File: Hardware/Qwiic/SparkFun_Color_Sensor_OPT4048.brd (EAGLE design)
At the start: 25.4 x 25.4 mm, 40 parts, among them J1 QWIIC_RIGHT_ANGLE, J2 QWIIC_RIGHT_ANGLE

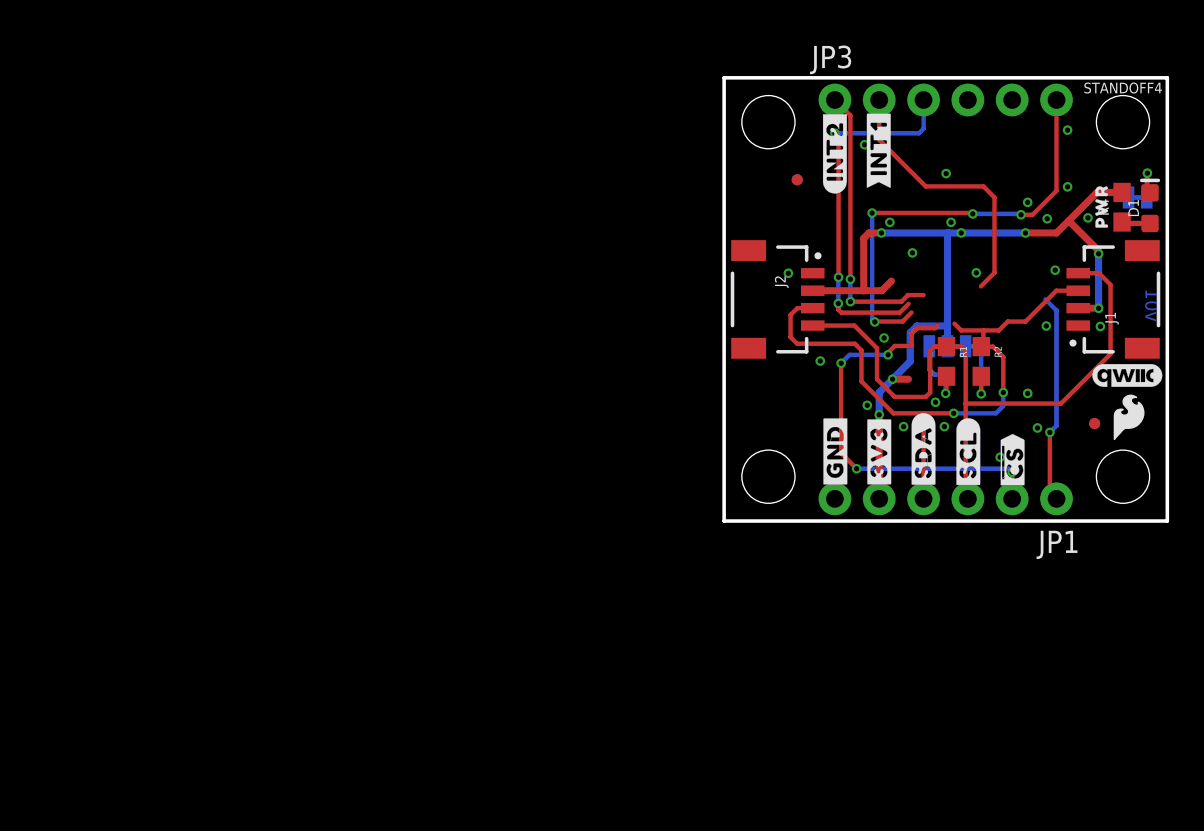
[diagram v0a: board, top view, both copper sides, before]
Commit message: Removes micro outline, adds mini outline
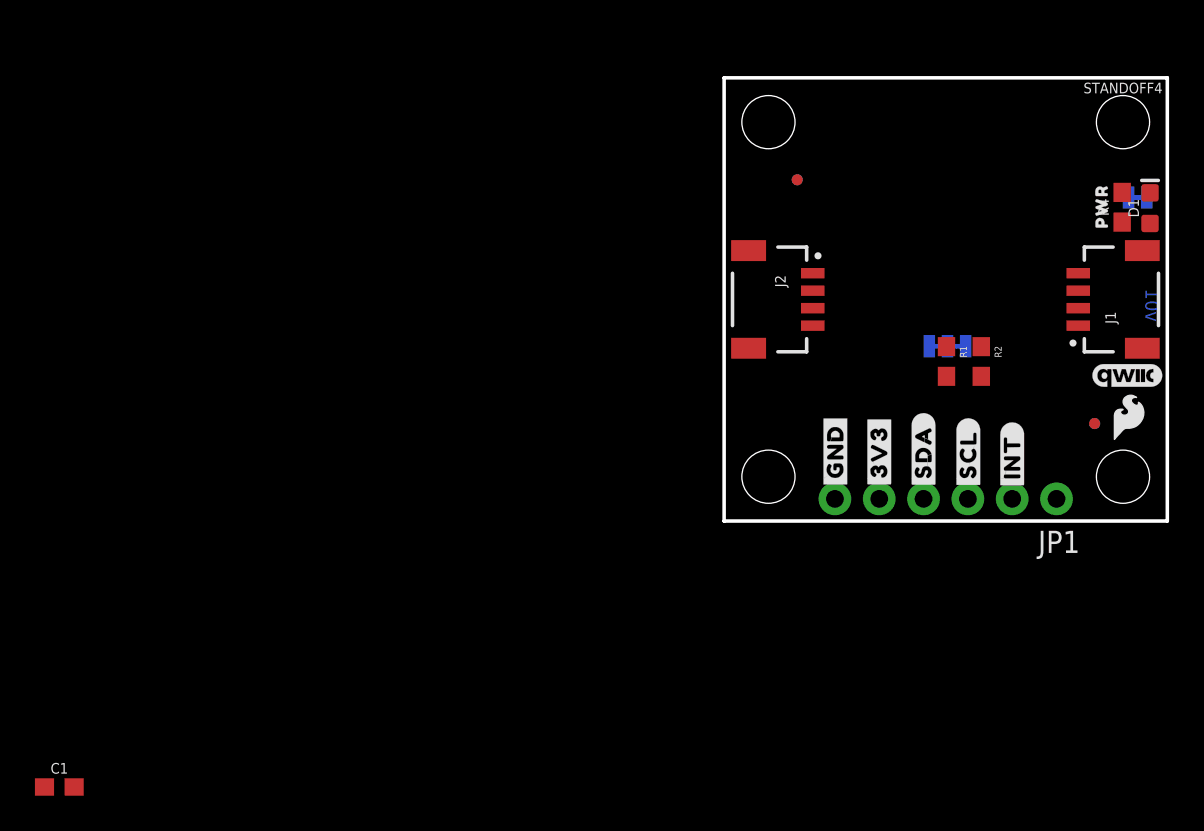
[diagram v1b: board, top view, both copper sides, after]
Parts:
- removed JP3: IO, SparkFun-Connectors:1X06_NO_SILK
- removed U$19: (no value), bot:#INT1#9
- removed U$26: (no value), ISMTop:#PICO#13
- removed U$27: (no value), bot:##CS##8
- removed U$40: (no value), top:#INT2#3
- removed U$8: (no value), top:#INT2#2
- added C1: 0.1uF, SparkFun-Capacitors:0603
- added U$6: (no value), bot:#INT#3
- U$3: device top:##CS##7 -> bot:#SDA#1
- U$7: device top:#INT1#9 -> top:#INT#9
- moved U$7 19.3 mm to (16.5, 3.68)
- moved U$3 5.14 mm to (11.4, 3.94), flipped to the bottom, turned to 270 degrees
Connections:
- net !CS! renamed INT
- net POCI/SA0 renamed ADDR
- net SDA/PICO renamed SDA
- removed net INT1: JP3.2
- removed net INT2: JP3.1
- removed net OCS: JP3.3
- removed net PICO_AUX: JP3.5
- removed net POCI_AUX: JP3.6
- removed net SCX: JP3.4
- net 3.3V: now also C1.1
- net GND: now also C1.2
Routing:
- net 3.3V: track 50.5 -> 0.00 mm, vias 7 -> 0
- net SCL: track 38.7 -> 0.00 mm
- net SDA: track 36.4 -> 0.00 mm, vias 2 -> 0
- net POCI_AUX: track 25.0 -> 0.00 mm, vias 4 -> 0
- net INT: track 23.8 -> 0.00 mm, vias 4 -> 0
- net OCS: track 21.3 -> 0.00 mm, vias 3 -> 0
- net INT2: track 16.3 -> 0.00 mm, vias 2 -> 0
- net INT1: track 15.7 -> 0.00 mm
- net ADDR: track 12.0 -> 0.00 mm, vias 1 -> 0
- net N$6: track 4.49 -> 0.00 mm, vias 1 -> 0
- net N$5: track 4.38 -> 0.00 mm, vias 1 -> 0
- net N$3: track 2.61 -> 0.00 mm, vias 1 -> 0
- net N$2: track 1.63 -> 0.00 mm
- net SCX: track 0.74 -> 0.00 mm
- net PICO_AUX: track 0.70 -> 0.00 mm

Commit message: Adds OPT4048 device, adds to Qwiic board
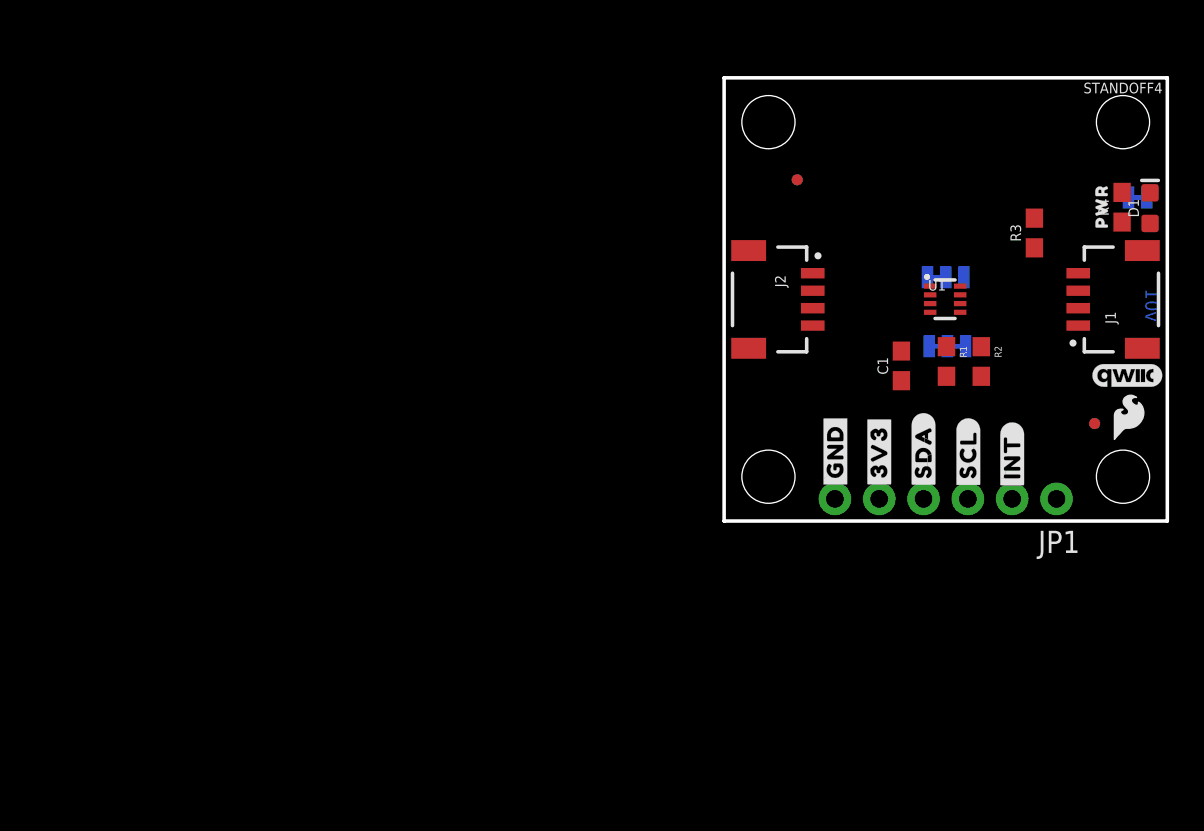
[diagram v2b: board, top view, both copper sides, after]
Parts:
- added ADDR: JUMPER-SMT_3_1-NC_TRACE_SILK, SparkFun-Jumpers:SMT-JUMPER_3_1-NC_TRACE_SILK
- added R3: 10k, SparkFun-Resistors:0603
- added U1: OPT4048, Color_Sensor:FCSOT
- moved C1 54.0 mm to (10.2, 8.89), turned to 90 degrees
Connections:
- new net N$1: R3.1, U1.P7
- net 3.3V: now also ADDR.1, R3.2, U1.P1
- net ADDR: now also ADDR.2, U1.P2
- net GND: now also ADDR.3, U1.P4
- net SCL: now also U1.P5
- net SDA: now also U1.P8
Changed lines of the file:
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@@
 <element name="U$6" library="bot" package="#INT#3" value="" x="16.51" y="3.683" smashed="yes" rot="MR270"/>
 <element name="U$7" library="top" package="#INT#9" value="" x="16.51" y="3.683" smashed="yes" rot="R90"/>
-<element name="C1" library="SparkFun-Capacitors" package="0603" value="0.1uF" x="-38.1" y="-15.24" smashed="yes">
-<attribute name="NAME" x="-38.1" y="-14.478" size="0.6096" layer="25" font="vector" ratio="20" align="bottom-center"/>
-<attribute name="PROD_ID" value="CAP-00810" x="-36.83" y="-15.24" size="1.778" layer="27" display="off"/>
-<attribute name="VALUE" x="-38.1" y="-16.002" size="0.6096" layer="27" font="vector" ratio="20" align="top-center"/>
+<element name="C1" library="SparkFun-Capacitors" package="0603" value="0.1uF" x="10.16" y="8.89" smashed="yes" rot="R90">
+<attribute name="NAME" x="9.398" y="8.89" size="0.6096" layer="25" font="vector" ratio="20" rot="R90" align="bottom-center"/>
+<attribute name="PROD_ID" value="CAP-00810" x="10.16" y="10.16" size="1.778" layer="27" rot="R90" display="off"/>
+<attribute name="VALUE" x="10.922" y="8.89" size="0.6096" layer="27" font="vector" ratio="20" rot="R90" align="top-center"/>
+</element>
+<element name="U1" library="Color_Sensor" package="FCSOT" value="OPT4048" x="12.7" y="12.7" smashed="yes">
+<attribute name="NAME" x="11.684" y="13.208" size="0.6096" layer="25" font="vector" ratio="20"/>
+<attribute name="PROD_ID" value="IC-8868" x="12.7" y="12.7" size="1.778" layer="27" display="off"/>
+<attribute name="VALUE" x="11.684" y="10.16" size="0.6096" layer="27" font="vector" ratio="20"/>
+</element>
+<element name="R3" library="SparkFun-Resistors" package="0603" value="10k" x="17.78" y="16.51" smashed="yes" rot="R90">
+<attribute name="NAME" x="17.018" y="16.51" size="0.6096" layer="25" font="vector" ratio="20" rot="R90" align="bottom-center"/>
+<attribute name="PROD_ID" value="RES-00824" x="17.78" y="16.51" size="1.778" layer="27" rot="R90" display="off"/>
+<attribute name="VALUE" value="10k" x="18.542" y="16.51" size="0.6096" layer="27" font="vector" ratio="20" rot="R90" align="top-center"/>
+</element>
+<element name="ADDR" library="SparkFun-Jumpers" package="SMT-JUMPER_3_1-NC_TRACE_SILK" package3d_urn="urn:adsk.eagle:package:39288/1" value="JUMPER-SMT_3_1-NC_TRACE_SILK" x="12.7" y="13.97" smashed="yes" rot="MR0">
+<attribute name="NAME" x="12.7" y="15.113" size="0.6096" layer="26" font="vector" ratio="20" rot="MR0" align="bottom-center"/>
+<attribute name="VALUE" x="12.7" y="12.827" size="0.6096" layer="28" font="vector" ratio="20" rot="MR0" align="top-center"/>
 </element>
 </elements>
@@
 <contactref element="LED" pad="1"/>
 <contactref element="C1" pad="2"/>
-<wire x1="6.35" y1="1.27" x2="-37.25" y2="-15.24" width="0" layer="19" extent="1-1"/>
-<wire x1="5.08" y1="14.2" x2="6.35" y2="1.27" width="0" layer="19" extent="1-1"/>
-<wire x1="20.2946" y1="11.2" x2="5.08" y2="14.2" width="0" layer="19" extent="1-1"/>
-<wire x1="23.1775" y1="18.542" x2="20.2946" y2="11.2" width="0" layer="19" extent="1-16"/>
+<contactref element="U1" pad="P4"/>
+<contactref element="ADDR" pad="3"/>
+<wire x1="20.2946" y1="11.2" x2="23.1775" y2="18.542" width="0" layer="19" extent="1-16"/>
+<wire x1="11.6586" y1="13.97" x2="20.2946" y2="11.2" width="0" layer="19" extent="1-16"/>
+<wire x1="11.811" y1="11.962" x2="11.6586" y2="13.97" width="0" layer="19" extent="1-16"/>
+<wire x1="10.16" y1="9.74" x2="11.6586" y2="13.97" width="0" layer="19" extent="1-16"/>
+<wire x1="5.08" y1="14.2" x2="11.6586" y2="13.97" width="0" layer="19" extent="1-16"/>
+<wire x1="6.35" y1="1.27" x2="10.16" y2="9.74" width="0" layer="19" extent="1-1"/>
 </signal>
 <signal name="SCL">
@@
 <contactref element="R1" pad="1"/>
 <contactref element="J2" pad="4"/>
-<wire x1="12.74445" y1="9.994" x2="20.2946" y2="14.2" width="0" layer="19" extent="1-1"/>
+<contactref element="U1" pad="P5"/>
+<wire x1="13.531" y1="11.962" x2="20.2946" y2="14.2" width="0" layer="19" extent="1-1"/>
+<wire x1="12.74445" y1="9.994" x2="13.531" y2="11.962" width="0" layer="19" extent="1-1"/>
 <wire x1="5.08" y1="11.2" x2="12.74445" y2="9.994" width="0" layer="19" extent="1-1"/>
 <wire x1="13.97" y1="1.27" x2="12.74445" y2="9.994" width="0" layer="19" extent="1-1"/>
@@
 <contactref element="R2" pad="1"/>
 <contactref element="J2" pad="3"/>
+<contactref element="U1" pad="P8"/>
 <wire x1="14.73835" y1="9.994" x2="20.2946" y2="13.2" width="0" layer="19" extent="1-1"/>
+<wire x1="13.531" y1="13.462" x2="14.73835" y2="9.994" width="0" layer="19" extent="1-1"/>
+<wire x1="5.08" y1="12.2" x2="13.531" y2="13.462" width="0" layer="19" extent="1-1"/>
 <wire x1="11.43" y1="1.27" x2="14.73835" y2="9.994" width="0" layer="19" extent="1-1"/>
-<wire x1="5.08" y1="12.2" x2="14.73835" y2="9.994" width="0" layer="19" extent="1-1"/>
 </signal>
 <signal name="INT">
@@
 <contactref element="R4" pad="2"/>
 <contactref element="C1" pad="1"/>
-<wire x1="8.89" y1="1.27" x2="-38.95" y2="-15.24" width="0" layer="19" extent="1-1"/>
-<wire x1="12.8016" y1="10.01395" x2="8.89" y2="1.27" width="0" layer="19" extent="16-16"/>
-<wire x1="20.2946" y1="12.2" x2="12.8016" y2="10.01395" width="0" layer="19" extent="1-16"/>
-<wire x1="22.8092" y1="18.8332" x2="20.2946" y2="12.2" width="0" layer="19" extent="1-1"/>
-<wire x1="5.08" y1="13.2" x2="12.8016" y2="10.01395" width="0" layer="19" extent="1-16"/>
+<contactref element="U1" pad="P1"/>
+<contactref element="R3" pad="2"/>
+<contactref element="ADDR" pad="1"/>
+<wire x1="17.78" y1="17.36" x2="22.8092" y2="18.8332" width="0" layer="19" extent="1-1"/>
+<wire x1="13.7414" y1="13.97" x2="17.78" y2="17.36" width="0" layer="19" extent="1-16"/>
+<wire x1="11.811" y1="13.462" x2="13.7414" y2="13.97" width="0" layer="19" extent="1-16"/>
+<wire x1="12.8016" y1="10.01395" x2="13.7414" y2="13.97" width="0" layer="19" extent="16-16"/>
+<wire x1="10.16" y1="8.04" x2="12.8016" y2="10.01395" width="0" layer="19" extent="1-16"/>
+<wire x1="20.2946" y1="12.2" x2="17.78" y2="17.36" width="0" layer="19" extent="1-1"/>
+<wire x1="8.89" y1="1.27" x2="10.16" y2="8.04" width="0" layer="19" extent="1-1"/>
+<wire x1="5.08" y1="13.2" x2="10.16" y2="8.04" width="0" layer="19" extent="1-1"/>
 </signal>
 <signal name="N$5">
@@
 <signal name="ADDR">
 <contactref element="JP1" pad="1"/>
+<contactref element="U1" pad="P2"/>
+<contactref element="ADDR" pad="2"/>
+<wire x1="12.7" y1="13.97" x2="11.811" y2="12.962" width="0" layer="19" extent="1-16"/>
+<wire x1="19.05" y1="1.27" x2="12.7" y2="13.97" width="0" layer="19" extent="16-16"/>
+</signal>
+<signal name="N$1">
+<contactref element="U1" pad="P7"/>
+<contactref element="R3" pad="1"/>
+<wire x1="13.531" y1="12.962" x2="17.78" y2="15.66" width="0" layer="19" extent="1-1"/>
 </signal>
 </signals>

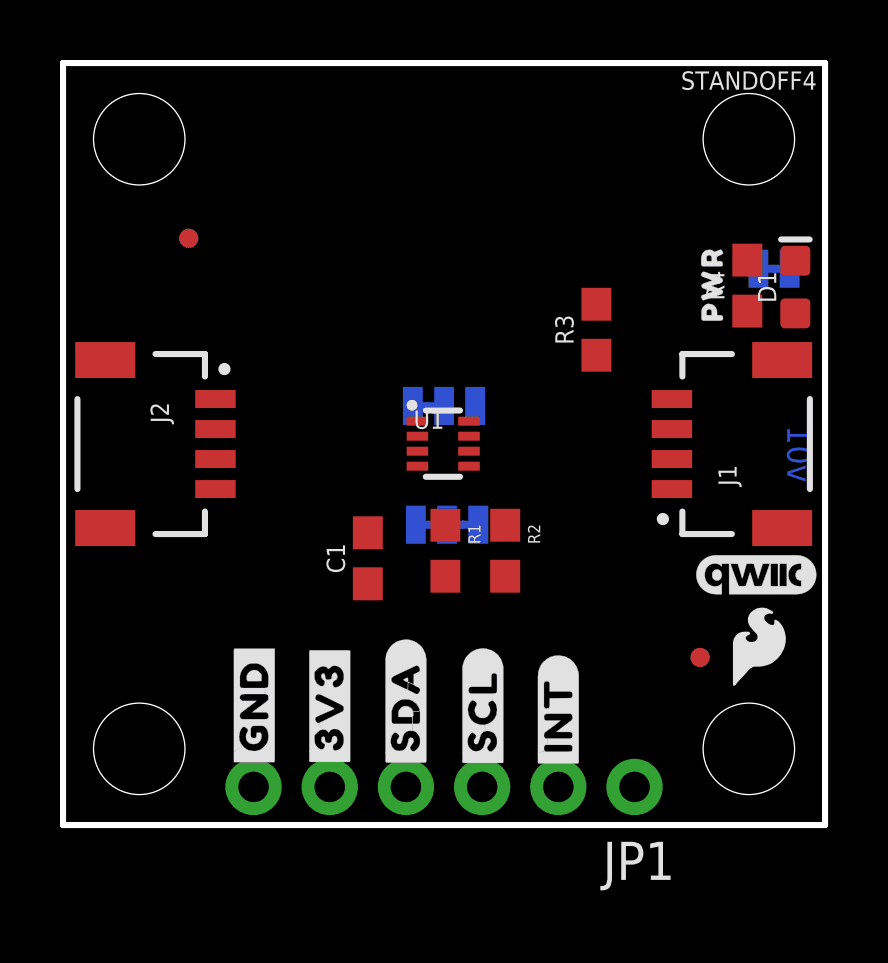
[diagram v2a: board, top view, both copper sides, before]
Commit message: Routes the Qwiic board
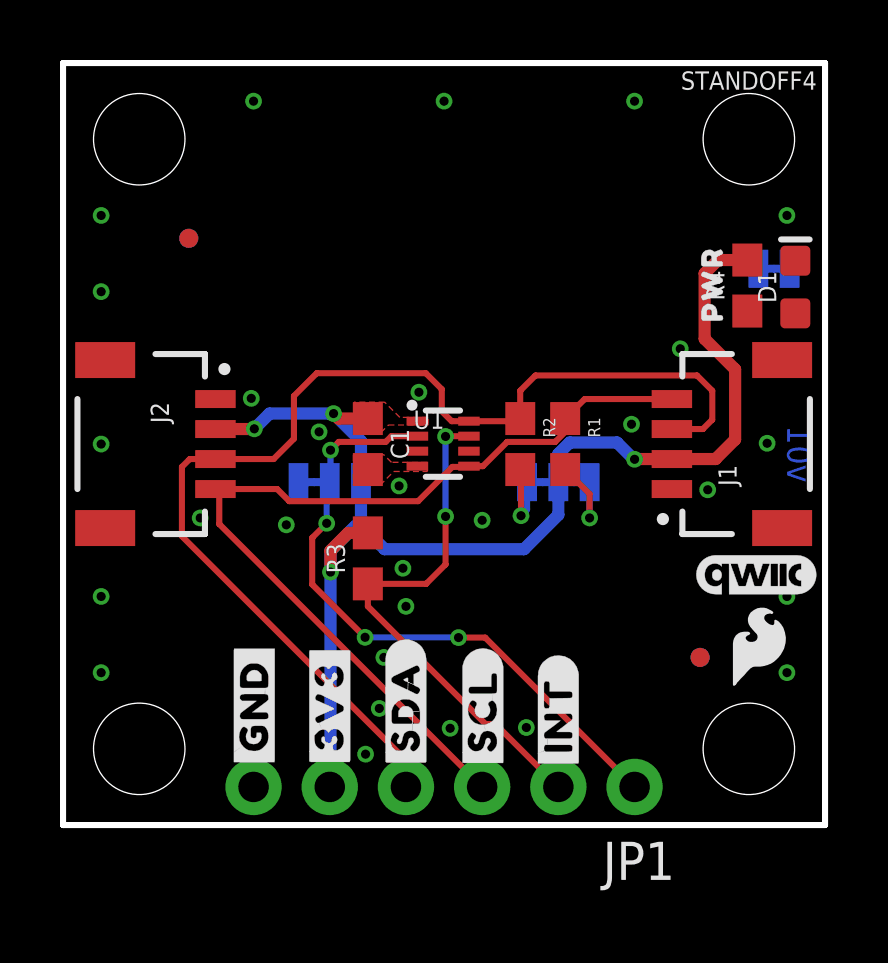
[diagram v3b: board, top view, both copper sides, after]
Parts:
- moved R3 10.8 mm to (10.2, 8.89)
- moved R1 5.35 mm to (16.7, 12.7)
- moved ADDR 4.58 mm to (8.89, 11.4)
- moved I2C_PU 3.97 mm to (16.5, 11.4), turned to 0 degrees
- moved U$25 3.96 mm to (16.5, 9.91)
- moved C1 3.81 mm to (10.2, 12.7), turned to 270 degrees
- moved R2 3.59 mm to (15.2, 12.7)
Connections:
- removed net N$1: R3.1, U1.P7
- net INT: now also R3.1, U1.P7
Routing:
- net 3.3V: track 0.00 -> 44.5 mm, vias 0 -> 4
- net SDA: track 0.00 -> 38.5 mm
- net SCL: track 0.00 -> 30.6 mm
- net ADDR: track 0.00 -> 21.4 mm, vias 0 -> 4
- net INT: track 0.00 -> 17.5 mm, vias 0 -> 2
- net N$5: track 0.00 -> 3.14 mm, vias 0 -> 1
- net N$6: track 0.00 -> 2.75 mm, vias 0 -> 1
- added copper zone on layer 1, net 3.3V
